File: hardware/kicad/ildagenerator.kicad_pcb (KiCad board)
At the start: 2 copper layers, 75.9 x 54.2 mm, 68 parts, among them P1 Out X, P2 Out Y, P3 Out Red, P4 Out Green, P5 Out Blue, P6 Out C1, P7 CONN_6, P8 CONN_4, U1 LTC2656BIFE-L16, U2 LT1356CN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

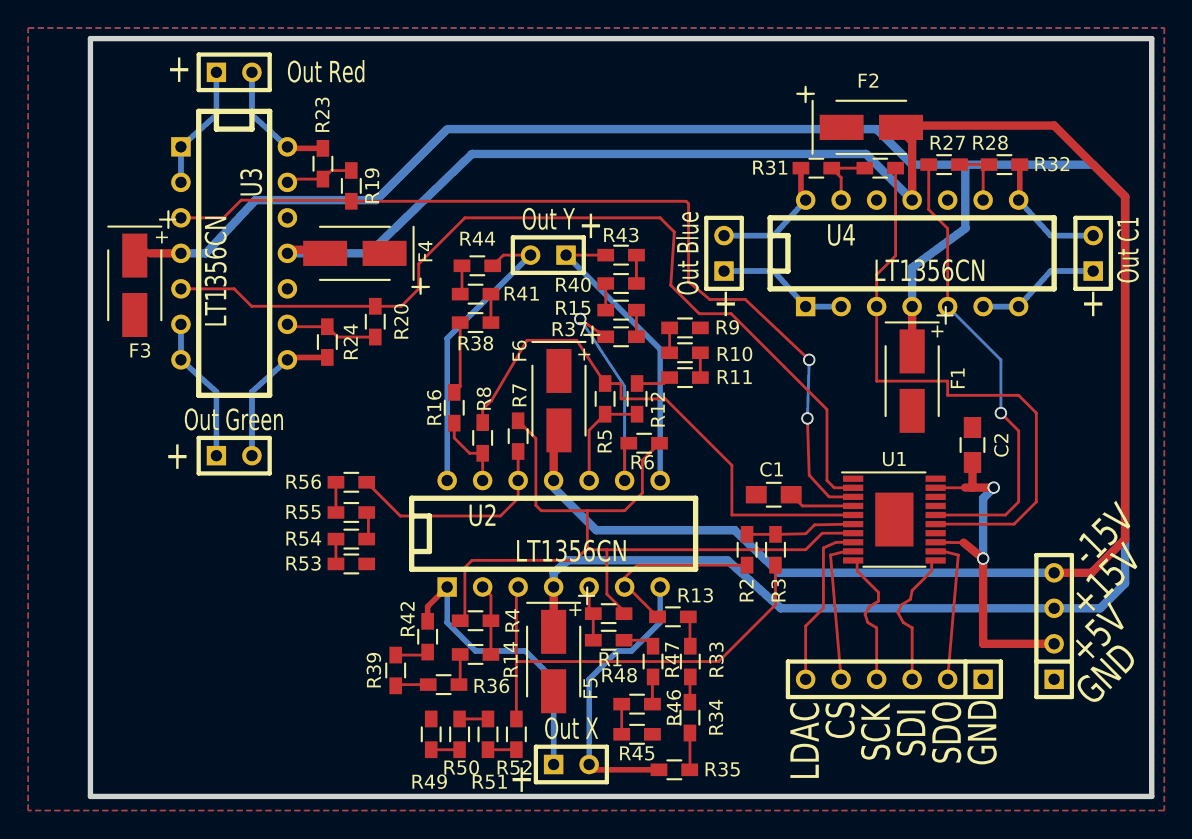
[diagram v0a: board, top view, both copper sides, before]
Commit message: rout output protection
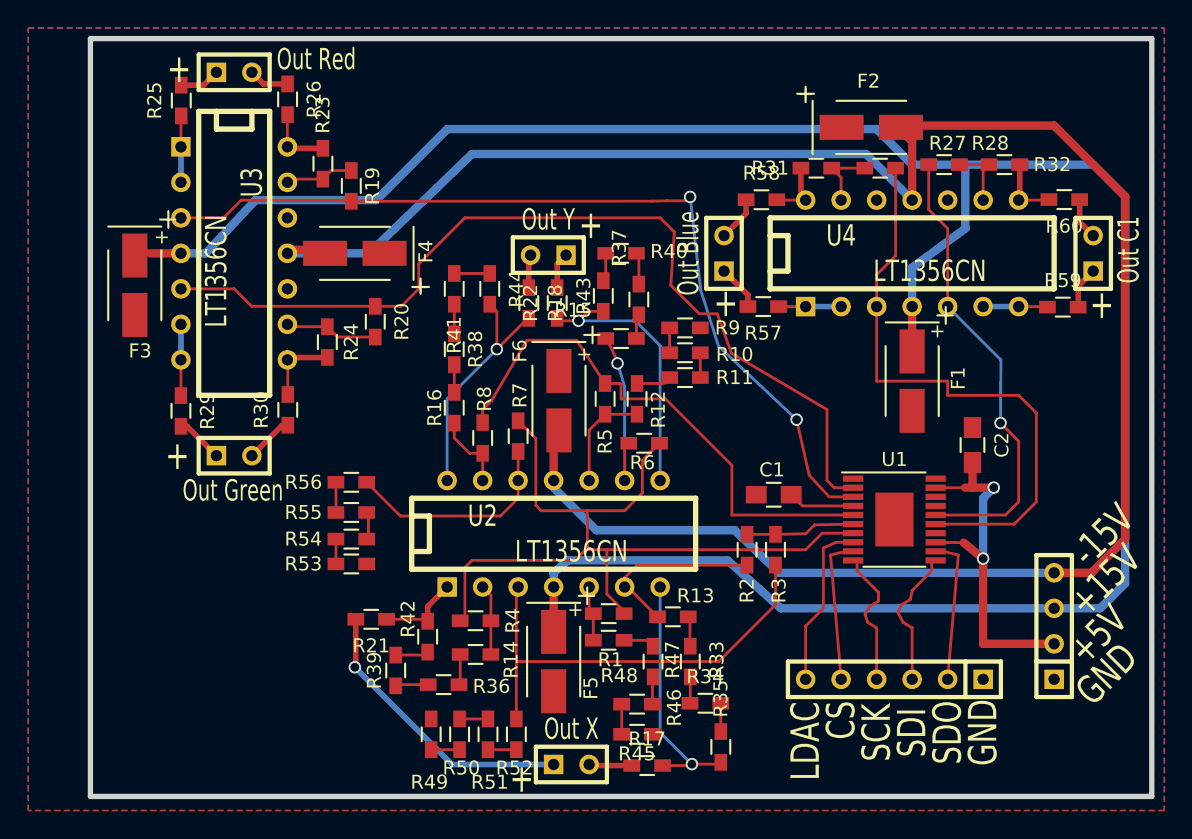
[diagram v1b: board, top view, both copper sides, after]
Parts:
- added R17: 10kΩ, Resistors_SMD:R_0603_HandSoldering, F.Cu at (142.3, 121.7)
- added R18: 10kΩ, Resistors_SMD:R_0603_HandSoldering, F.Cu at (133.9, 88.6)
- added R21: 10kΩ, Resistors_SMD:R_0603_HandSoldering, F.Cu at (122.6, 111.3)
- added R22: 10kΩ, Resistors_SMD:R_0603_HandSoldering, F.Cu at (135.9, 88.6)
- added R25: 10kΩ, Resistors_SMD:R_0603_HandSoldering, F.Cu at (109.0, 74.2)
- added R26: 10kΩ, Resistors_SMD:R_0603_HandSoldering, F.Cu at (116.6, 74.1)
- added R29: 10kΩ, Resistors_SMD:R_0603_HandSoldering, F.Cu at (109.0, 96.4)
- added R30: 10kΩ, Resistors_SMD:R_0603_HandSoldering, F.Cu at (116.6, 96.3)
- added R57: 10kΩ, Resistors_SMD:R_0603_HandSoldering, F.Cu at (150.6, 88.9)
- added R58: 10kΩ, Resistors_SMD:R_0603_HandSoldering, F.Cu at (150.5, 81.3)
- added R59: 10kΩ, Resistors_SMD:R_0603_HandSoldering, F.Cu at (172.1, 88.9)
- added R60: 10kΩ, Resistors_SMD:R_0603_HandSoldering, F.Cu at (172.2, 81.2)
- moved R35 3.71 mm to (147.6, 120.4), turned to 270 degrees
- moved R43 3.19 mm to (139.2, 88.1), turned to 270 degrees
- moved R38 2.44 mm to (128.5, 91.9), turned to 90 degrees
- moved R40 2.16 mm to (140.5, 85.1), turned to 180 degrees
- moved R44 1.88 mm to (131.1, 87.6), turned to 270 degrees
- moved R41 1.57 mm to (128.5, 87.6), turned to 90 degrees
- moved R34 1.51 mm to (146.5, 117.3), turned to 0 degrees
- moved R37 1.48 mm to (141.7, 88.4), turned to 90 degrees
- moved R15 0.13 mm to (140.5, 91.2)
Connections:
- R23 pad 2: Net-(P3-Pad2) -> Net-(R23-Pad2)
- R24 pad 2: Net-(P4-Pad2) -> Net-(R24-Pad2)
- R31 pad 2: Net-(P5-Pad2) -> Net-(R31-Pad2)
- R32 pad 2: Net-(P6-Pad2) -> Net-(R32-Pad2)
- R35 pad 2: Net-(P1-Pad2) -> Net-(R17-Pad2)
- R42 pad 2: Net-(P1-Pad1) -> Net-(R21-Pad1)
- R43 pad 2: Net-(P2-Pad1) -> Net-(R22-Pad1)
- R44 pad 2: Net-(P2-Pad2) -> Net-(R18-Pad2)
- U2 pad 1: Net-(P1-Pad1) -> Net-(R21-Pad1)
- U2 pad 14: Net-(P2-Pad2) -> Net-(R18-Pad2)
- U2 pad 7: Net-(P1-Pad2) -> Net-(R17-Pad2)
- U2 pad 8: Net-(P2-Pad1) -> Net-(R22-Pad1)
- U3 pad 1: Net-(P3-Pad1) -> Net-(R25-Pad1)
- U3 pad 14: Net-(P3-Pad2) -> Net-(R23-Pad2)
- U3 pad 2: Net-(P3-Pad1) -> Net-(R25-Pad1)
- U3 pad 6: Net-(P4-Pad1) -> Net-(R29-Pad1)
- U3 pad 7: Net-(P4-Pad1) -> Net-(R29-Pad1)
- U3 pad 8: Net-(P4-Pad2) -> Net-(R24-Pad2)
- U4 pad 1: Net-(P5-Pad1) -> Net-(R57-Pad1)
- U4 pad 14: Net-(P5-Pad2) -> Net-(R31-Pad2)
- U4 pad 2: Net-(P5-Pad1) -> Net-(R57-Pad1)
- U4 pad 6: Net-(P6-Pad1) -> Net-(R59-Pad1)
- U4 pad 7: Net-(P6-Pad1) -> Net-(R59-Pad1)
- U4 pad 8: Net-(P6-Pad2) -> Net-(R32-Pad2)
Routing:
- net Net-(R22-Pad1): track 0.00 -> 19.9 mm, vias 0 -> 1
- net Net-(P2-Pad1): track 21.9 -> 2.59 mm
- net Net-(P2-Pad2): track 21.6 -> 2.38 mm
- net Net-(R17-Pad2): track 0.00 -> 18.3 mm, vias 0 -> 1
- net Net-(P1-Pad2): track 21.0 -> 3.08 mm
- net Net-(R18-Pad2): track 0.00 -> 17.5 mm, vias 0 -> 1
- net Net-(P4-Pad2): track 10.9 -> 3.47 mm
- net Net-(P4-Pad1): track 10.5 -> 3.41 mm
- net Net-(P3-Pad2): track 9.30 -> 2.90 mm
- net Net-(P5-Pad1): track 9.51 -> 3.25 mm
- net Net-(P5-Pad2): track 9.40 -> 3.22 mm
- net Net-(P3-Pad1): track 9.01 -> 2.90 mm
- net Net-(P6-Pad2): track 9.04 -> 2.98 mm
- net Net-(R21-Pad1): track 0.00 -> 6.03 mm
- net Net-(P6-Pad1): track 9.01 -> 3.02 mm
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
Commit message: mov output protect
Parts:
- added MOV1: 5.6V, Resistors_SMD:R_1206_HandSoldering, F.Cu at (116.8, 111.3)
- added MOV10: 5.6V, Resistors_SMD:R_1206_HandSoldering, F.Cu at (148.3, 76.7)
- added MOV11: 5.6V, Resistors_SMD:R_1206_HandSoldering, F.Cu at (173.2, 94.5)
- added MOV12: 5.6V, Resistors_SMD:R_1206_HandSoldering, F.Cu at (176.3, 78.2)
- added MOV2: 5.6V, Resistors_SMD:R_1206_HandSoldering, F.Cu at (150.4, 123.4)
- added MOV3: 5.6V, Resistors_SMD:R_1206_HandSoldering, F.Cu at (136.7, 80.3)
- added MOV4: 5.6V, Resistors_SMD:R_1206_HandSoldering, F.Cu at (133.6, 80.3)
- added MOV5: 5.6V, Resistors_SMD:R_1206_HandSoldering, F.Cu at (105.2, 100.1)
- added MOV6: 5.6V, Resistors_SMD:R_1206_HandSoldering, F.Cu at (122.4, 97.0)
- added MOV7: 5.6V, Resistors_SMD:R_1206_HandSoldering, F.Cu at (105.2, 75.2)
- added MOV8: 5.6V, Resistors_SMD:R_1206_HandSoldering, F.Cu at (122.9, 73.2)
- added MOV9: 5.6V, Resistors_SMD:R_1206_HandSoldering, F.Cu at (152.9, 91.4)
- R17, R18, R21, R22, R25, R26, R29, R30, R57, R58, R59, R60: value 10kΩ -> 470Ω
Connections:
- U4 pad 11: -15V -> Net-(U4-Pad11)
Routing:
- net -15V: track 149.2 -> 105.3 mm
- net Net-(MOV12-Pad1): track 2.98 -> 38.1 mm
- net Net-(U4-Pad11): track 0.00 -> 8.86 mm
- net (no net): track 0.00 -> 3.05 mm

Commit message: placing movs
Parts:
- moved R17 4.62 mm to (146.3, 119.4)
- moved MOV2 3.87 mm to (146.8, 121.9)
- moved MOV12 3.61 mm to (173.5, 75.9)
- moved R35 3.10 mm to (148.6, 117.5), turned to 180 degrees
- moved R34 2.71 mm to (148.6, 115.6)
- moved MOV5 2.27 mm to (106.2, 102.1)
- moved MOV6 2.27 mm to (121.4, 99.1)
- moved MOV11 1.02 mm to (173.2, 93.5)
- moved MOV8 0.76 mm to (122.2, 73.2)
- moved MOV9 0.51 mm to (152.4, 91.4)
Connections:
- U4 pad 11: Net-(U4-Pad11) -> -15V
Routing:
- net -15V: track 105.3 -> 153.8 mm
- net Net-(MOV12-Pad1): track 38.1 -> 6.36 mm
- net Net-(U4-Pad11): track 8.86 -> 0.00 mm
- net Net-(MOV2-Pad1): track 3.08 -> 9.55 mm
- net Net-(MOV6-Pad1): track 3.47 -> 9.04 mm
- net Net-(MOV5-Pad2): track 3.41 -> 8.97 mm
- net Net-(R17-Pad2): track 18.3 -> 13.8 mm
- net Net-(MOV7-Pad2): track 2.90 -> 6.78 mm
- net Net-(MOV8-Pad1): track 2.90 -> 6.55 mm
- net Net-(MOV4-Pad1): track 2.38 -> 5.49 mm
- net (no net): track 3.05 -> 0.00 mm
- net Net-(MOV3-Pad2): track 2.59 -> 5.60 mm
- net Net-(MOV10-Pad1): track 3.22 -> 6.21 mm
- net Net-(MOV9-Pad2): track 3.25 -> 6.15 mm
- net Net-(MOV1-Pad2): track 20.6 -> 23.2 mm
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
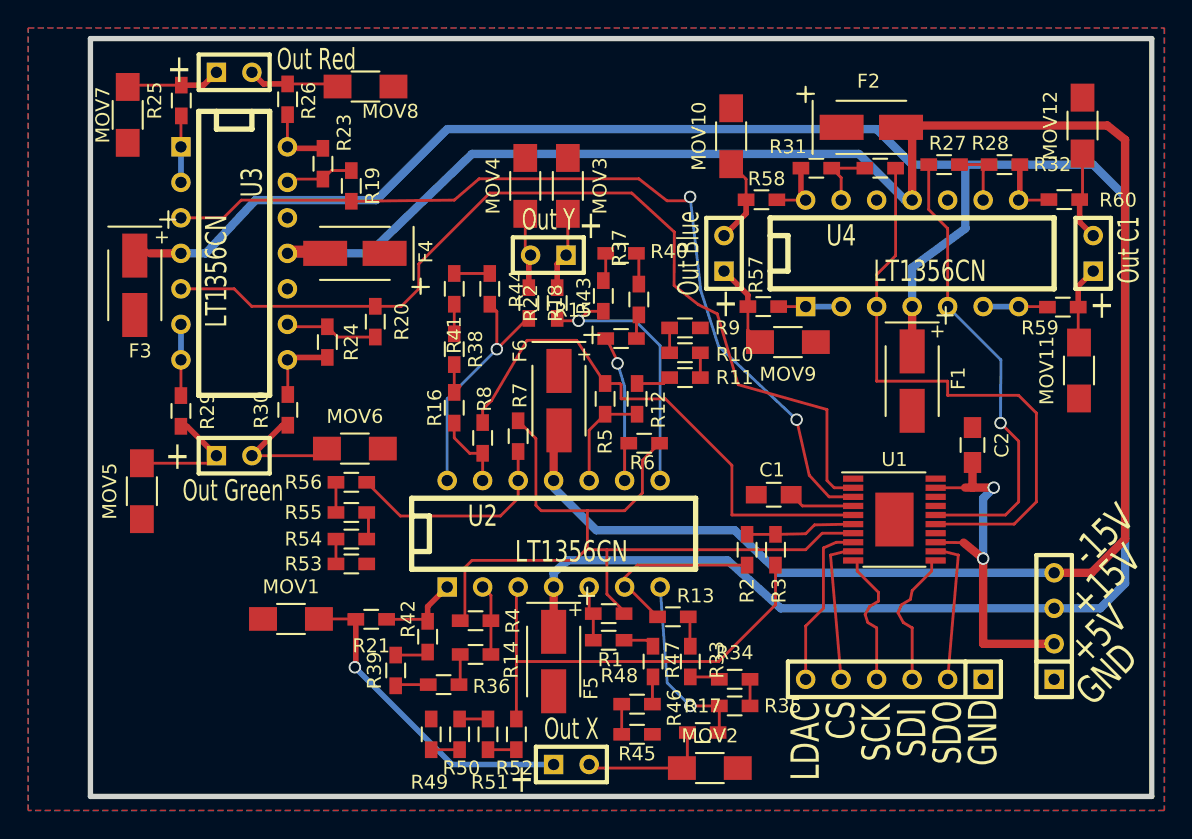
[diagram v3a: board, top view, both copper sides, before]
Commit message: onboard power dc/dc
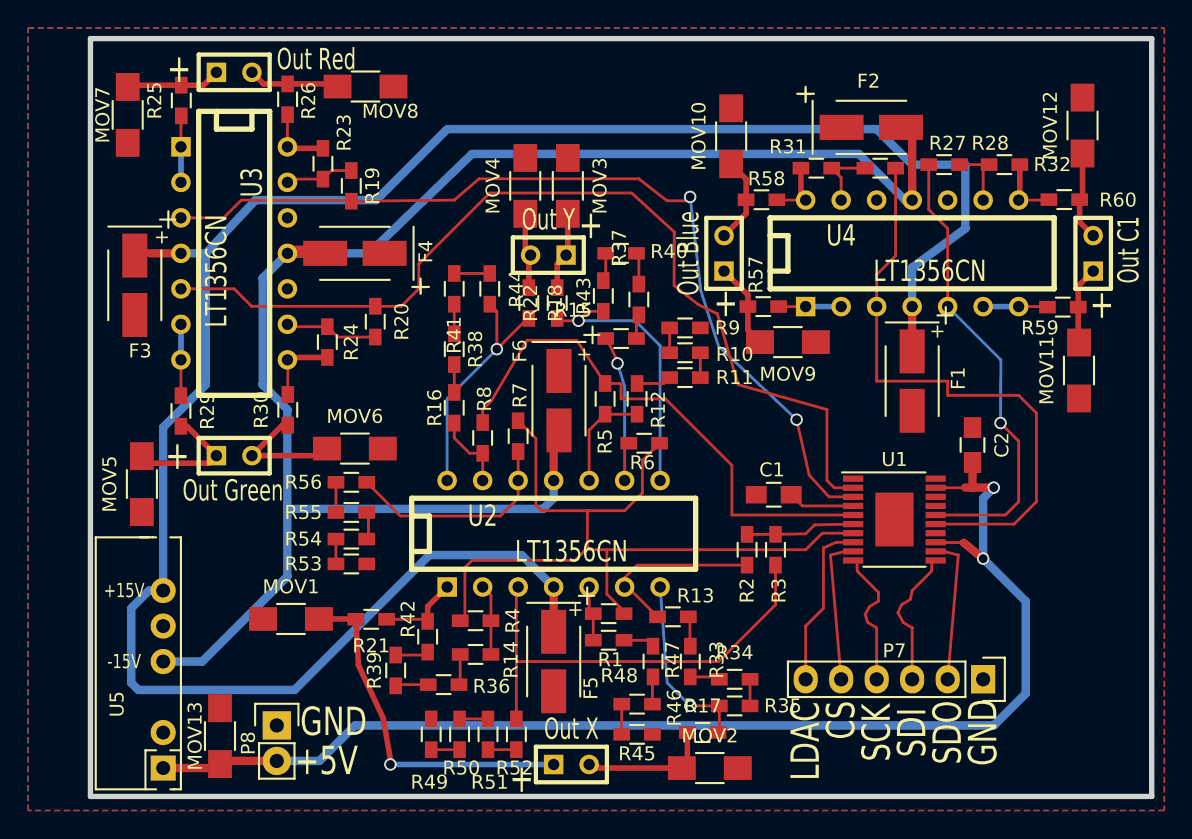
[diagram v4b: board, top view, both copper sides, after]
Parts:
- added MOV13: 5.6V, Resistors_SMD:R_1206_HandSoldering, F.Cu at (111.8, 119.6)
- added U5: NMA0509SC, footprints:NMA_5V_12V_15V_Series, F.Cu at (107.7, 111.8)
- P7: footprint SIL-6 -> Pin_Headers:Pin_Header_Straight_1x06
- P8: footprint SIL-4 -> Pin_Headers:Pin_Header_Straight_1x02
- moved P8 56.1 mm to (115.8, 118.9), turned to 0 degrees
- moved P7 6.35 mm to (166.4, 115.6), turned to 270 degrees
- moved MOV5 0.51 mm to (106.2, 101.6)
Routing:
- net +5V: track 26.6 -> 90.3 mm
- net -15V: track 153.8 -> 121.2 mm
- net +15V: track 166.9 -> 151.5 mm
- net Net-(MOV1-Pad2): track 23.2 -> 24.9 mm

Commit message: correct socket
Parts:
- moved MOV5 4.06 mm to (106.2, 97.5), turned to 270 degrees
- moved U5 2.62 mm to (105.4, 113.0)
- moved MOV13 1.05 mm to (112.8, 119.9)
- moved P8 1.02 mm to (116.8, 118.9)
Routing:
- net +5V: track 90.3 -> 93.1 mm
- net -15V: track 121.2 -> 123.0 mm
- net +15V: track 151.5 -> 152.8 mm
